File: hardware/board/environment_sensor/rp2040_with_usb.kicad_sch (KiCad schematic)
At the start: 43 parts, among them J2 AudioJack3, J3 USB_C_Receptacle_USB2.0, SW1 SW_Push, U1 TPD2EUSB30, U2 LP2985-3.3, U3 RP2040, U4 W25Q16JVUXIQ, X1 ECS-TXO-2016

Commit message: draft v0.1 pcb
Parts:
- C4: Link https://www.digikey.com/en/products/detail/yageo/CC0402KPX7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 -> https://www.digikey.com/en/products/detail/murata-electroni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; Manufacturer Yageo -> Murata Electronics; Manufacturer Number CC0402KPX7R8BB103 -> GRM1555C1E103GE01D; Temperature Coefficient X7R -> COG/NP0; Tolerance 10% -> 2%; Vendor Number (none) -> 490-GRM1555C1E103GE01DDKR-ND
- D5: Link (none) -> https://www.digikey.com/en/products/detail/nexperia-usa-inc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; PCBWay Link (none) -> https://www.pcbway.com/components/detail/BAT54J115/291478/
- J2: Alternate SJ-3523-SMT-TR -> (none); Manufacturer Number SJ-3524-SMT-TR-BE -> SJ-3523-SMT-TR
- R1: Link https://www.digikey.com/en/products/detail/yageo/RT0402BRD0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 -> https://www.digikey.com/en/products/detail/yageo/AC0402FR-1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; Manufacturer Number RT0402BRD071KL -> AC0402FR-131KL
- U2: Link (none) -> https://www.digikey.com/en/products/detail/texas-instrument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
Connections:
- net +3V3: now also C4.1; no longer C4.2
- net CS: now also U3.31 (GPIO20); no longer U3.8 (GPIO6)
- net GND: now also C4.2; no longer C4.1
- net PICO: now also U3.30 (GPIO19); no longer U3.5 (GPIO3)
- net POCI: now also U3.27 (GPIO16); no longer U3.6 (GPIO4)
- net SCK: now also U3.29 (GPIO18); no longer U3.4 (GPIO2)
- net SWCLK: no longer names the net of U3.24 (SWCLK)
- net SWDIO: no longer names the net of U3.25 (SWD)
- net UART0_RXD: no longer names the net of U3.3 (GPIO1)
- net UART0_TXD: no longer names the net of U3.2 (GPIO0)
- no-connect marks 25 -> 29
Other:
- note added: "SPIO CS"
- note added: "SPIO RX"
- note added: "SPIO SCK"
- note added: "SPIO TX"
- note removed: "(SPIO)"
- moved on the sheet: C22, D5

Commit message: update 3.5mm connector orientation and 3d models
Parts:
- D4: PCBWay Link (none) -> https://www.pcbway.com/components/detail/XZCDGK53W1VF/50198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
- FID1, FID2, FID3: PCBWay Link (none) -> n/a
- R8: Notes DNP -> (none); Tolerance (none) -> 1%
- U2: Link https://www.digikey.com/en/products/detail/texas-instruments/LP2985AIM5X-3-3-NOPB/367668 -> https://www.digikey.com/en/products/detail/texas-instruments/LP2985-33DBVR/809759; Manufacturer Number LP2985AIM5X-3.3/NOPB -> LP2985-33DBVR; PCBWay Link (none) -> https://www.pcbway.com/components/detail/LP298533DBVR/56728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
- X1: PCBWay Link (none) -> https://www.pcbway.com/components/detail/ECSTXO201633120TR/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
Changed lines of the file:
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@@
       (effects (font (size 1.27 1.27)) hide)
     )
-    (property "Notes" "DNP" (at 243.205 27.305 0)
+    (property "Notes" "" (at 243.205 27.305 0)
+      (effects (font (size 1.27 1.27)) hide)
+    )
+    (property "Tolerance" "1%" (at 243.205 27.305 0)
       (effects (font (size 1.27 1.27)) hide)
     )
@@
       (effects (font (size 1.27 1.27)) hide)
     )
+    (property "PCBWay Link" "https://www.pcbway.com/components/detail/ECSTXO201633120TR/348903/" (at 160.02 109.855 0)
+      (effects (font (size 1.27 1.27)) hide)
+    )
     (pin "1")
     (pin "2")
@@
       (effects (font (size 1.27 1.27)) hide)
     )
+    (property "PCBWay Link" "n/a" (at 274.955 151.765 0)
+      (effects (font (size 1.27 1.27)) hide)
+    )
     (instances
       (project "environment_sensor"
@@
       (effects (font (size 1.27 1.27)) hide)
     )
+    (property "PCBWay Link" "https://www.pcbway.com/components/detail/XZCDGK53W1VF/501988/" (at 268.605 139.7 0)
+      (effects (font (size 1.27 1.27)) hide)
+    )
     (pin "1")
     (pin "2")
@@
       (effects (font (size 1.27 1.27)) hide)
     )
-    (property "Manufacturer Number" "LP2985AIM5X-3.3/NOPB" (at 127 31.75 0)
+    (property "Manufacturer Number" "LP2985-33DBVR" (at 127 31.75 0)
+      (effects (font (size 1.27 1.27)) hide)
+    )
+    (property "Link" "https://www.digikey.com/en/products/detail/texas-instruments/LP2985-33DBVR/809759" (at 127 31.75 0)
       (effects (font (size 1.27 1.27)) hide)
     )
-    (property "Link" "https://www.digikey.com/en/products/detail/texas-instruments/LP2985AIM5X-3-3-NOPB/367668" (at 127 31.75 0)
+    (property "PCBWay Link" "https://www.pcbway.com/components/detail/LP298533DBVR/567284/" (at 127 31.75 0)
       (effects (font (size 1.27 1.27)) hide)
     )
@@
       (effects (font (size 1.27 1.27)) hide)
     )
+    (property "PCBWay Link" "n/a" (at 274.955 156.845 0)
+      (effects (font (size 1.27 1.27)) hide)
+    )
     (instances
       (project "environment_sensor"
@@
       (effects (font (size 1.27 1.27)) hide)
     )
+    (property "PCBWay Link" "n/a" (at 274.955 161.925 0)
+      (effects (font (size 1.27 1.27)) hide)
+    )

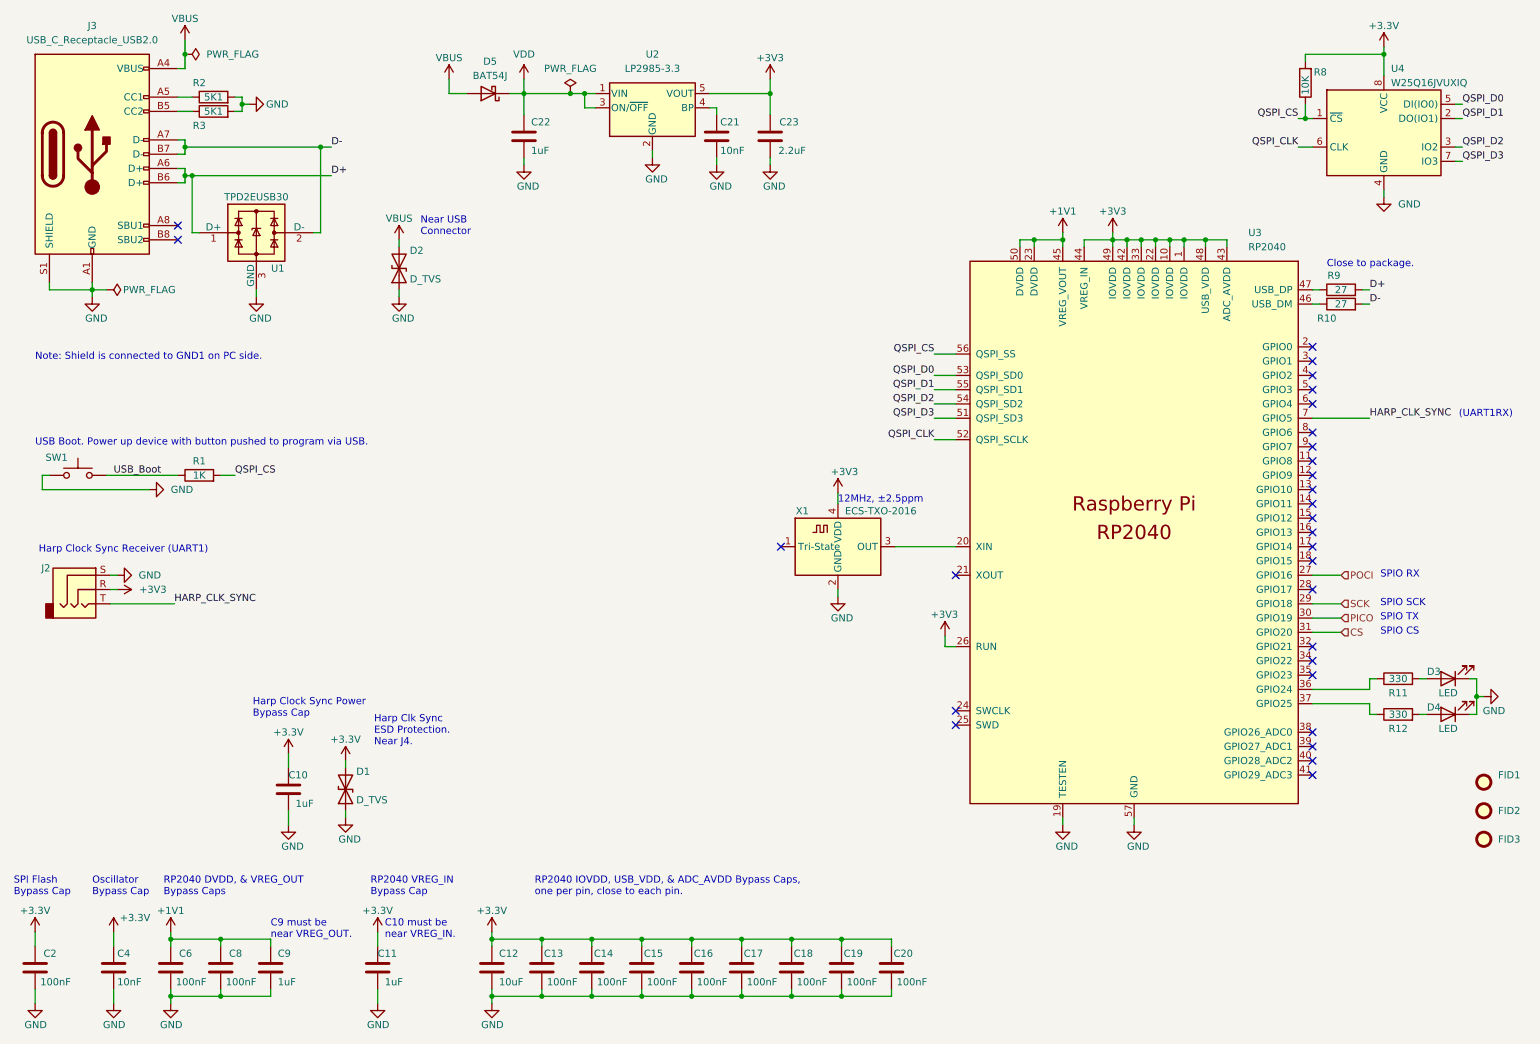
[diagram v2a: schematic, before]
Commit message: update pcb with thermal considerations
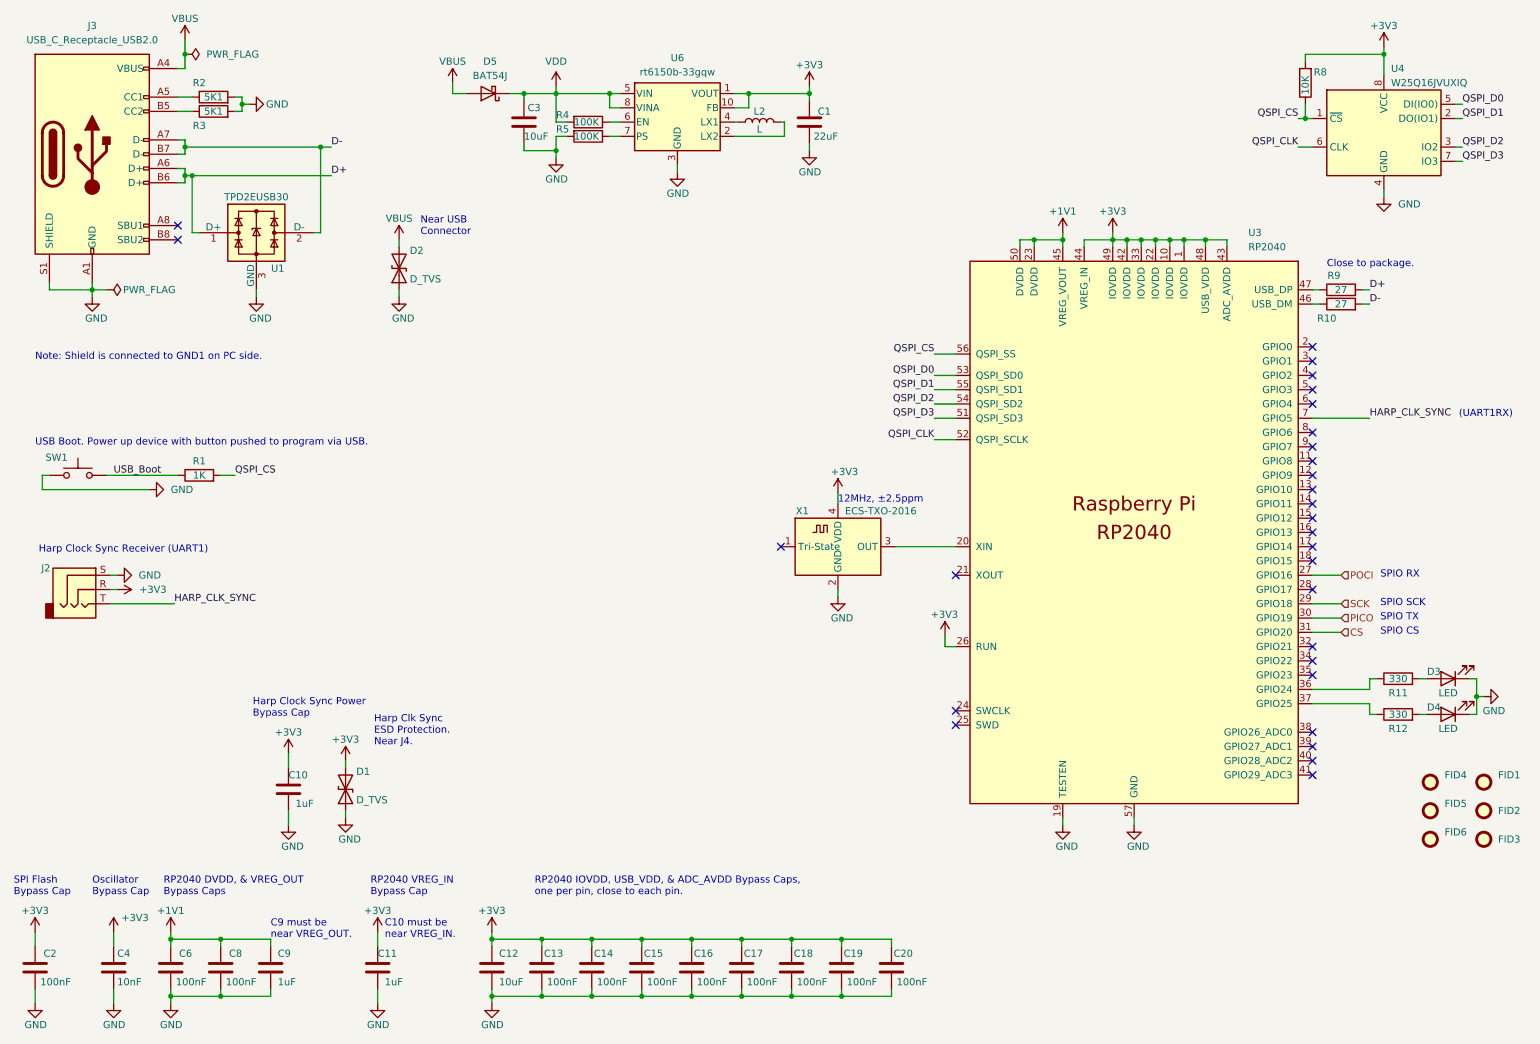
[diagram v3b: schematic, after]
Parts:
- removed C21: 10nF, Capacitor_SMD:C_0402_1005Metric, symbol Device:C
- removed C22: 1uF, Capacitor_SMD:C_0402_1005Metric, symbol Device:C
- removed C23: 2.2uF, Capacitor_SMD:C_0402_1005Metric, symbol Device:C
- removed U2: LP2985-3.3, Package_TO_SOT_SMD:SOT-23-5, symbol Regulator_Linear:LP2985-3.3
- added C1: 22uF, Capacitor_SMD:C_0805_2012Metric, symbol Device:C
- added C3: 10uF, Capacitor_SMD:C_0805_2012Metric, symbol Device:C
- added FID4, FID5, FID6: Fiducial, Fiducial:Fiducial_0.5mm_Mask1mm, symbol Mechanical:Fiducial
- added L2: L, Inductor_SMD:L_0603_1608Metric, symbol Device:L
- added R4, R5: 100K, Resistor_SMD:R_0402_1005Metric, symbol Device:R
- added U6: rt6150b-33gqw, kicad_component_library:WDFN-10-1EP_2.5x2.5mm_P0.5_EP1.25x2.1mm, symbol kicad_component_library:rt6150b-33gqw
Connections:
- net +3V3: now also C1.2, U6.1 (VOUT), U6.10 (FB)
- net GND: now also C1.1, C3.2, R5.2, U6.11 (GND), U6.3 (GND), U6.9 (GND)
- net VDD: now also C3.1, R4.2, U6.5 (VIN), U6.8 (VINA)
- new net: L2.2, U6.2 (LX2)
- new net: L2.1, U6.4 (LX1)
- new net: R4.1, U6.6 (EN)
- new net: R5.1, U6.7 (PS)

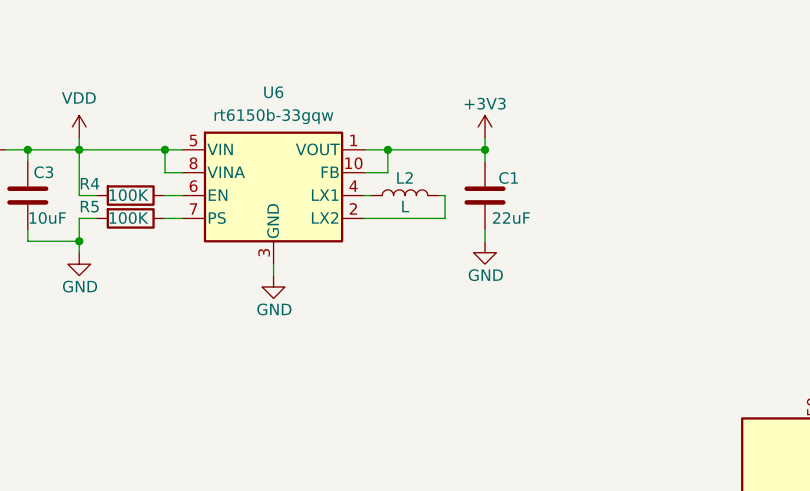
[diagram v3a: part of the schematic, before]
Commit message: update pcb thermal landing
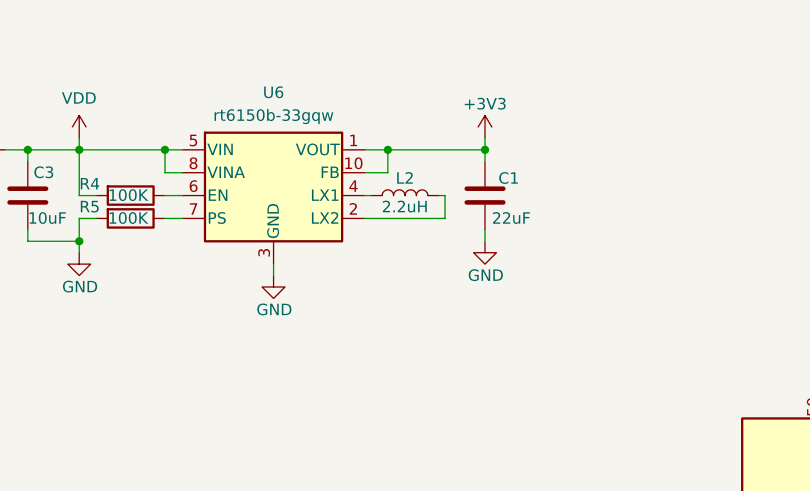
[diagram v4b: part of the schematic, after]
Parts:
- L2: value L -> 2.2uH; DC Resistance (none) -> 1.5Ohm
- R4, R5: Link (none) -> https://www.digikey.com/en/products/detail/yageo/RC0402FR-0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; Manufacturer (none) -> Yageo; Manufacturer Number (none) -> RC0402FR-07100KL
- U6: Link (none) -> https://www.digikey.com/en/products/detail/richtek-usa-inc/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; Manufacturer (none) -> Richtek USA Inc.; Manufacturer Number (none) -> RT6150B-33GQW
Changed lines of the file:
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@@
 			)
 		)
+		(property "Manufacturer" "Richtek USA Inc."
+			(at 131.445 31.75 0)
+			(effects
+				(font
+					(size 1.27 1.27)
+				)
+				(hide yes)
+			)
+		)
+		(property "Manufacturer Number" "RT6150B-33GQW"
+			(at 131.445 31.75 0)
+			(effects
+				(font
+					(size 1.27 1.27)
+				)
+				(hide yes)
+			)
+		)
+		(property "Link" "https://www.digikey.com/en/products/detail/richtek-usa-inc/RT6150B-33GQW/6676709"
+			(at 131.445 31.75 0)
+			(effects
+				(font
+					(size 1.27 1.27)
+				)
+				(hide yes)
+			)
+		)
 		(pin "4"
 		)
@@
 			)
 		)
-		(property "Datasheet" ""
+		(property "Datasheet" "https://www.yageo.com/upload/media/product/products/datasheet/rchip/PYu-RC_Group_51_RoHS_L_12.pdf"
 			(at 115.57 36.83 0)
 			(effects
@@
 			)
 		)
-		(property "Link" ""
+		(property "Link" "https://www.digikey.com/en/products/detail/yageo/RC0402FR-07100KL/726526"
 			(at 115.57 36.83 90)
 			(effects
@@
 			)
 		)
-		(property "Manufacturer" ""
-			(at 115.57 36.83 0)
-			(effects
-				(font
-					(size 1.27 1.27)
-				)
-				(hide yes)
-			)
-		)
-		(property "Manufacturer Number" ""
+		(property "Manufacturer" "Yageo"
 			(at 115.57 36.83 0)
 			(effects
@@
 			)
 		)
-		(property "Notes" ""
+		(property "Manufacturer Number" "RC0402FR-07100KL"
 			(at 115.57 36.83 0)
 			(effects
@@
 			)
 		)
-		(property "Value" "L"
+		(property "Value" "2.2uH"
 			(at 146.05 35.56 90)
 			(effects
@@
 			)
 		)
+		(property "DC Resistance" "1.5Ohm"
+			(at 146.05 34.29 90)
+			(effects
+				(font
+					(size 1.27 1.27)
+				)
+				(hide yes)
+			)
+		)
 		(pin "2"
 		)
@@
 			)
 		)
-		(property "Datasheet" ""
+		(property "Datasheet" "https://www.yageo.com/upload/media/product/products/datasheet/rchip/PYu-RC_Group_51_RoHS_L_12.pdf"
 			(at 115.57 34.29 0)
 			(effects
@@
 			)
 		)
-		(property "Link" ""
+		(property "Link" "https://www.digikey.com/en/products/detail/yageo/RC0402FR-07100KL/726526"
 			(at 115.57 34.29 90)
 			(effects
@@
 			)
 		)
-		(property "Manufacturer" ""
-			(at 115.57 34.29 0)
-			(effects
-				(font
-					(size 1.27 1.27)
-				)
-				(hide yes)
-			)
-		)
-		(property "Manufacturer Number" ""
+		(property "Manufacturer" "Yageo"
 			(at 115.57 34.29 0)
 			(effects
@@
 			)
 		)
-		(property "Notes" ""
+		(property "Manufacturer Number" "RC0402FR-07100KL"
 			(at 115.57 34.29 0)
 			(effects

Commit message: update CUI -> Same Sky
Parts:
- J2: footprint Connector_Audio:Jack_3.5mm_CUI_SJ-3523-SMT_Horizontal -> Connector_Audio:Jack_3.5mm_CUI_SJ-3524-SMT_Horizontal; Alternate (none) -> SJ-3524-SMT-TR-GR; Link https://www.digikey.com/en/products/detail/cui-devices/SJ-3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 -> https://www.digikey.com/en/products/detail/same-sky-formerl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; Manufacturer (none) -> Same Sky; Manufacturer Number SJ-3523-SMT-TR -> SJ-3524-SMT-TR; PCBWay Link https://www.pcbway.com/components/detail/SJ3523SMTTR/473228/ -> (none)
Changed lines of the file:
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@@
 			)
 		)
-		(property "Footprint" "Connector_Audio:Jack_3.5mm_CUI_SJ-3523-SMT_Horizontal"
+		(property "Footprint" "Connector_Audio:Jack_3.5mm_CUI_SJ-3524-SMT_Horizontal"
 			(at 25.4 117.475 0)
 			(effects
@@
 			)
 		)
-		(property "Datasheet" "https://www.cuidevices.com/product/resource/sj-352x-smt.pdf"
+		(property "Datasheet" "https://www.cuhttps://www.sameskydevices.com/product/resource/sj-352x-smt.pdfidevices.com/product/resource/sj-352x-smt.pdf"
 			(at 25.4 117.475 0)
 			(effects
@@
 			)
 		)
-		(property "Link" "https://www.digikey.com/en/products/detail/cui-devices/SJ-3524-SMT-TR-BE/2295987"
+		(property "Link" "https://www.digikey.com/en/products/detail/same-sky-formerly-cui-devices/SJ-3524-SMT-TR/281298"
 			(at 25.4 117.475 0)
 			(effects
@@
 			)
 		)
-		(property "PCBWay Link" "https://www.pcbway.com/components/detail/SJ3523SMTTR/473228/"
+		(property "Manufacturer Number" "SJ-3524-SMT-TR"
 			(at 25.4 117.475 0)
 			(effects
@@
 			)
 		)
-		(property "Manufacturer Number" "SJ-3523-SMT-TR"
+		(property "Alternate" "SJ-3524-SMT-TR-GR"
 			(at 25.4 117.475 0)
 			(effects
@@
 			)
 		)
-		(property "Alternate" ""
+		(property "Manufacturer" "Same Sky"
 			(at 25.4 117.475 0)
 			(effects
